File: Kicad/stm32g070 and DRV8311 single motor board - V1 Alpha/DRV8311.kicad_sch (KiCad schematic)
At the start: 10 parts, among them J3 Molex_PicoBlade_53048-0310 Ho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, U2 DRV8311HRRWR

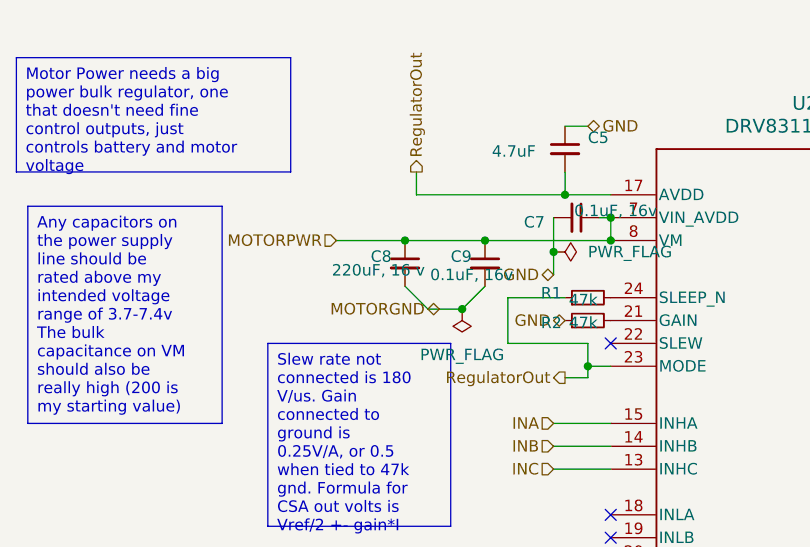
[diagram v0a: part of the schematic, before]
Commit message: Fixes to the PCB after production related to mosfets
So..... I sourced the wrong mosfets. I chose mosfets with the marketing moniker PowerPAK, never thinking that could mean multiple footprint sizes. I sourced mosfets with the powerpak 1212 footprint, instead of the powerpak SO-8 footprint. They ended up being tiny and I had to do a bodge fix to test. I have replaced the mosfets in schematic with correctly sized ones now.

Another change I made in this commit is related to LEDs. I sourced the leds and resistors last minute, so the values are a bit different than originally on the schematic. I realized too that my tri-state led status circuit wouldn't work, because the bq25060 status pin is not a tri-state and I couldn't make it one. I now only have one led to indicate charging. I have updated the schematics and board with the values and single status led.

The big capacitors I sourced differently, I wasn't able to get a small 220uF, so I got a big aluminum polarized 220uF and put it in place of the 1000uF. All the other capacitors are different too, I realized the voltage rating doesn't matter on some, so to cut down BOM part number if there was a capacitor value with two separate voltages, I just went with 16v one.

Gerber files have been updated.
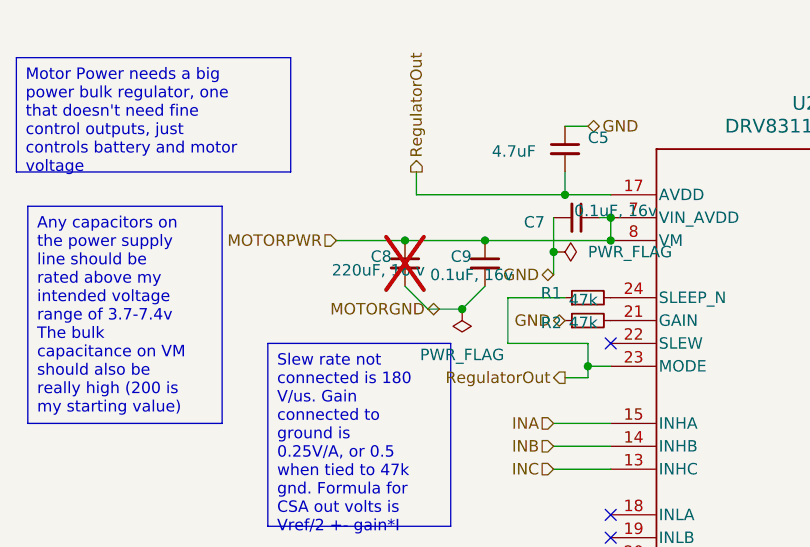
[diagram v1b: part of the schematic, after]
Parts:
- C8: now not fitted; now left out of the parts list
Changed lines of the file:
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@@
 		(unit 1)
 		(exclude_from_sim no)
-		(in_bom yes)
+		(in_bom no)
 		(on_board yes)
-		(dnp no)
+		(dnp yes)
 		(property "Reference" "C8"
 			(at 81.28 61.468 0)

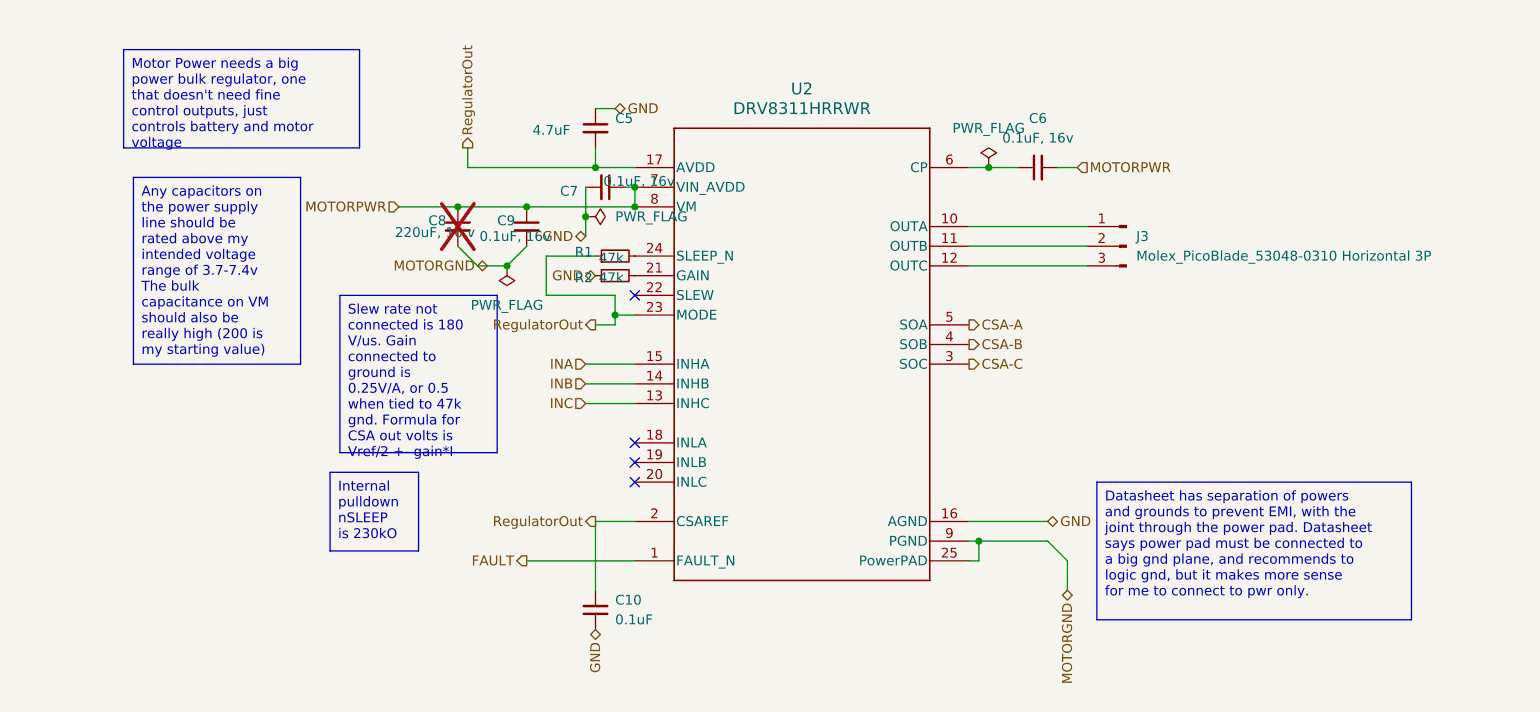
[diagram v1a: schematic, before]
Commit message: Fixing DRV8311 recursive design flaw, and pin tie issue
Since I'm using 3x pwm mode for the driver, I should have tied the unused lowside pins to 3.3v, and not left them floating, according to the datasheet. This is fixed now

The driver chip has an enable pin with an internal weak pulldown. I put a pull-up resistor on the outside, to always keep the chip on. Guess what that is connected to though? The regulator output from the chip, which is disabled! I fixed this in the design by have a voltage divider coming from motor power to enable the pin.
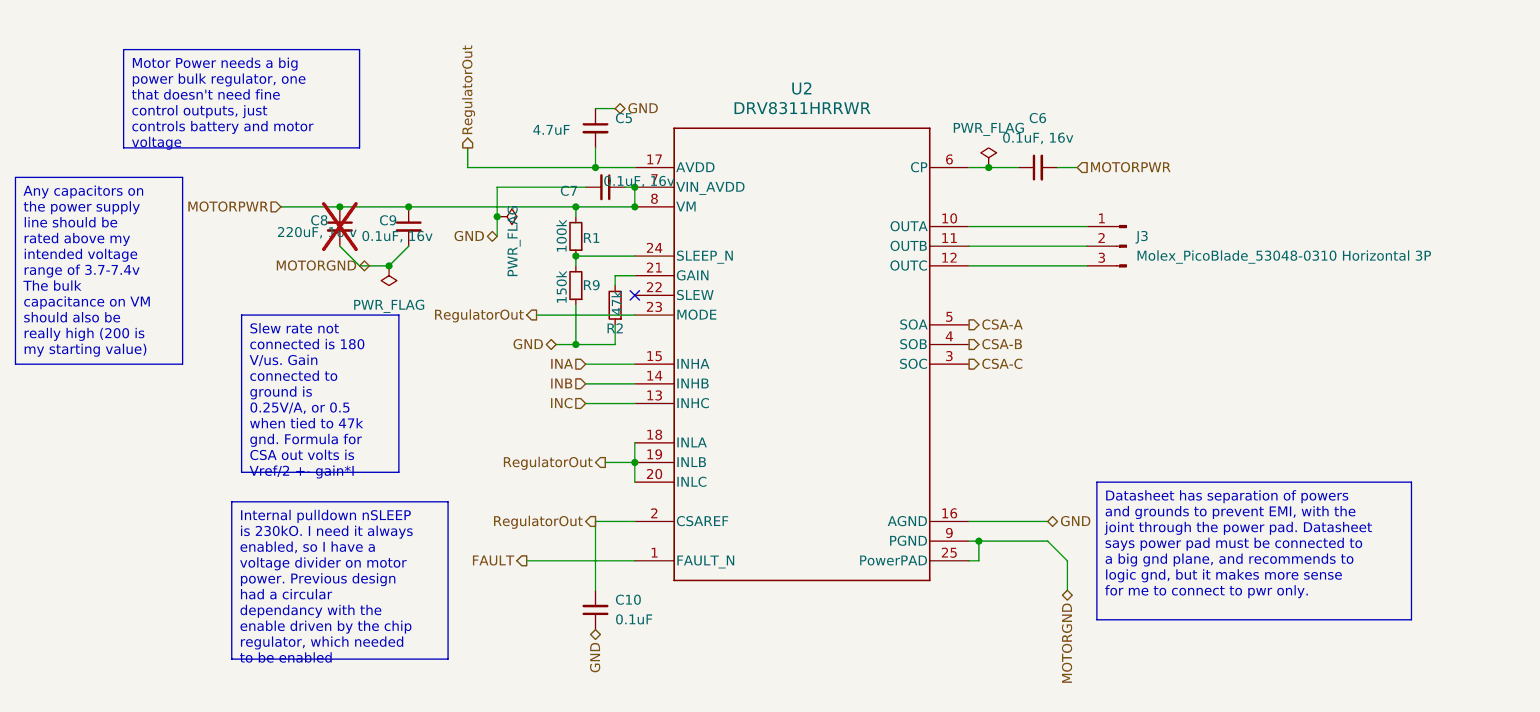
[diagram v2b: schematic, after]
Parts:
- added R9: 150k, Resistor_SMD:R_0603_1608Metric, symbol Device:R_Small
- R1: value 47k -> 100k
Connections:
- net GND: now also R9.1
- net MOTORPWR: now also R1.2
- net RegulatorOut: now also U2.18 (INLA), U2.19 (INLB), U2.20 (INLC); no longer R1.1
- net at U2.24 (SLEEP_N): now also R1.1, R9.2; no longer R1.2
- no-connect marks 4 -> 1
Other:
- moved on the sheet: C8, C9, R1, R2
